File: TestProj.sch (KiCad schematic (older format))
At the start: 28 parts, among them SW1 SW_Push, U1 ATmega32U4-AU, Y1 16MHz

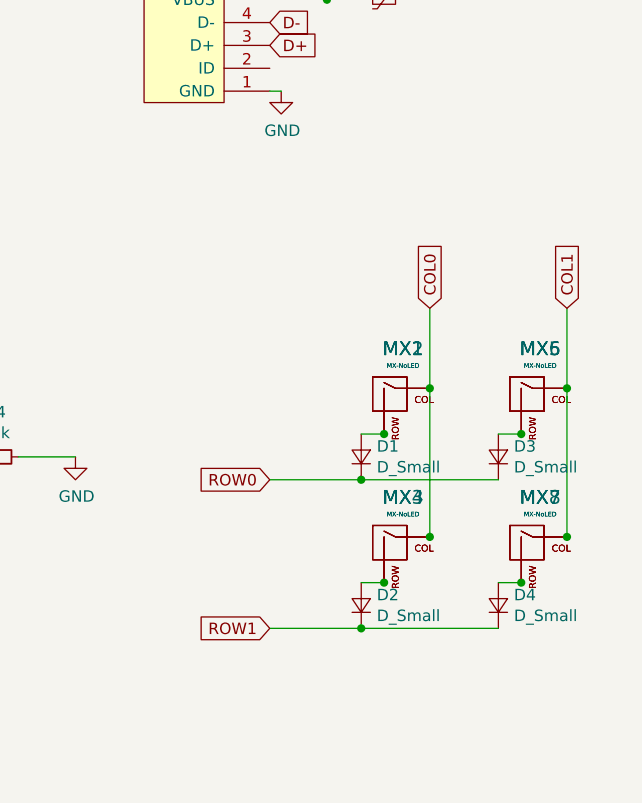
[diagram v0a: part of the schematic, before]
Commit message: fix dupe switches
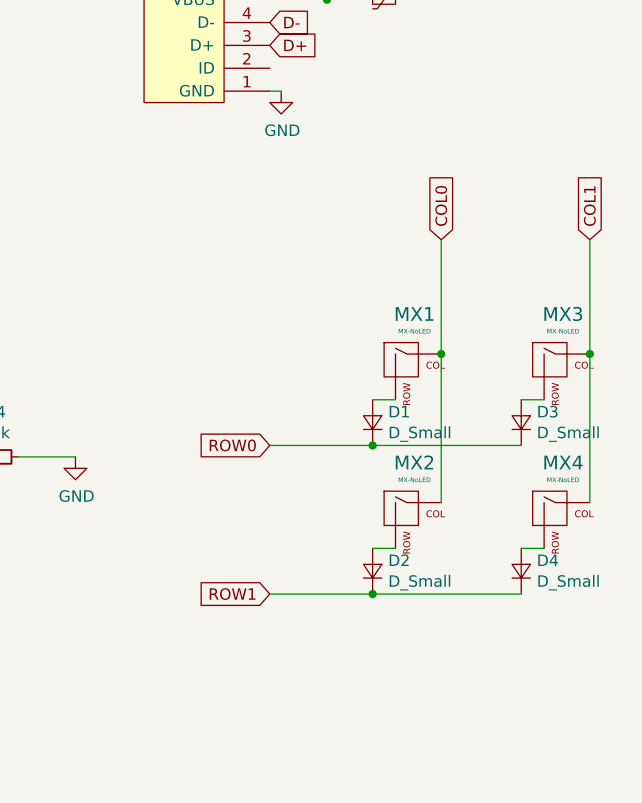
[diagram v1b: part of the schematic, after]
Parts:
- removed MX5, MX6, MX7, MX8: MX-NoLED, MX_Only:MXOnly-1U, symbol MX_Alps_Hybrid:MX-NoLED
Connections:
- net COL0: no longer MX3.1 (COL), MX4.1 (COL)
- net COL1: now also MX3.1 (COL), MX4.1 (COL)
- net at D1.2 (A), MX1.2 (ROW): no longer MX2.2 (ROW)
- net at D4.2 (A): now also MX4.2 (ROW)
- net at D3.2 (A): now also MX3.2 (ROW)
- new net: D2.2 (A), MX2.2 (ROW)
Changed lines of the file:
@@
 Wire Wire Line
 	7000 2750 7050 2750
-Connection ~ 7500 4900
+$Comp
+L MX_Alps_Hybrid:MX-NoLED MX1
+U 1 1 5D524996
+P 7600 3950
+F 0 "MX1" H 7633 4173 60  0000 C CNN
+F 1 "MX-NoLED" H 7633 4099 20  0000 C CNN
+F 2 "MX_Only:MXOnly-1U" H 6975 3925 60  0001 C CNN
+F 3 "" H 6975 3925 60  0001 C CNN
+	1    7600 3950
+	1    0    0    -1
+$EndComp
+$Comp
+L Device:D_Small D1
+U 1 1 5D52500E
+P 7450 4200
+F 0 "D1" V 7496 4132 50  0000 R CNN
+F 1 "D_Small" V 7405 4132 50  0000 R CNN
+F 2 "Diode_SMD:D_SOD-123" V 7450 4200 50  0001 C CNN
+F 3 "~" V 7450 4200 50  0001 C CNN
+	1    7450 4200
+	0    -1   -1   0
+$EndComp
+Wire Wire Line
+	7550 4100 7450 4100
+$Comp
+L MX_Alps_Hybrid:MX-NoLED MX2
+U 1 1 5D526ECD
+P 7600 4600
+F 0 "MX2" H 7633 4823 60  0000 C CNN
+F 1 "MX-NoLED" H 7633 4749 20  0000 C CNN
+F 2 "MX_Only:MXOnly-1U" H 6975 4575 60  0001 C CNN
+F 3 "" H 6975 4575 60  0001 C CNN
+	1    7600 4600
+	1    0    0    -1
+$EndComp
+$Comp
+L Device:D_Small D2
+U 1 1 5D526ED7
+P 7450 4850
+F 0 "D2" V 7496 4782 50  0000 R CNN
+F 1 "D_Small" V 7405 4782 50  0000 R CNN
+F 2 "Diode_SMD:D_SOD-123" V 7450 4850 50  0001 C CNN
+F 3 "~" V 7450 4850 50  0001 C CNN
+	1    7450 4850
+	0    -1   -1   0
+$EndComp
+Wire Wire Line
+	7550 4750 7450 4750
+$Comp
+L MX_Alps_Hybrid:MX-NoLED MX3
+U 1 1 5D528B54
+P 8250 3950
+F 0 "MX3" H 8283 4173 60  0000 C CNN
+F 1 "MX-NoLED" H 8283 4099 20  0000 C CNN
+F 2 "MX_Only:MXOnly-1U" H 7625 3925 60  0001 C CNN
+F 3 "" H 7625 3925 60  0001 C CNN
+	1    8250 3950
+	1    0    0    -1
+$EndComp
+$Comp
+L Device:D_Small D3
+U 1 1 5D528B5E
+P 8100 4200
+F 0 "D3" V 8146 4132 50  0000 R CNN
+F 1 "D_Small" V 8055 4132 50  0000 R CNN
+F 2 "Diode_SMD:D_SOD-123" V 8100 4200 50  0001 C CNN
+F 3 "~" V 8100 4200 50  0001 C CNN
+	1    8100 4200
+	0    -1   -1   0
+$EndComp
+Wire Wire Line
+	8200 4100 8100 4100
 $Comp
 L MX_Alps_Hybrid:MX-NoLED MX4
-U 1 1 5D4EFD87
-P 7550 4750
-F 0 "MX4" H 7583 4973 60  0000 C CNN
-F 1 "MX-NoLED" H 7583 4899 20  0000 C CNN
-F 2 "MX_Only:MXOnly-1U" H 6925 4725 60  0001 C CNN
-F 3 "" H 6925 4725 60  0001 C CNN
-	1    7550 4750
+U 1 1 5D528B69
+P 8250 4600
+F 0 "MX4" H 8283 4823 60  0000 C CNN
+F 1 "MX-NoLED" H 8283 4749 20  0000 C CNN
+F 2 "MX_Only:MXOnly-1U" H 7625 4575 60  0001 C CNN
+F 3 "" H 7625 4575 60  0001 C CNN
+	1    8250 4600
 	1    0    0    -1
 $EndComp
-Wire Wire Line
-	7500 4900 7400 4900
 $Comp
-L Device:D_Small D2
-U 1 1 5D4EFD7C
-P 7400 5000
-F 0 "D2" V 7446 4932 50  0000 R CNN
-F 1 "D_Small" V 7355 4932 50  0000 R CNN
-F 2 "Diode_SMD:D_SOD-123" V 7400 5000 50  0001 C CNN
-F 3 "~" V 7400 5000 50  0001 C CNN
-	1    7400 5000
+L Device:D_Small D4
+U 1 1 5D528B73
+P 8100 4850
+F 0 "D4" V 8146 4782 50  0000 R CNN
+F 1 "D_Small" V 8055 4782 50  0000 R CNN
+F 2 "Diode_SMD:D_SOD-123" V 8100 4850 50  0001 C CNN
+F 3 "~" V 8100 4850 50  0001 C CNN
+	1    8100 4850
 	0    -1   -1   0
 $EndComp
-$Comp
-L MX_Alps_Hybrid:MX-NoLED MX3
-U 1 1 5D4EFD72
-P 7550 4750
-F 0 "MX3" H 7583 4973 60  0000 C CNN
-F 1 "MX-NoLED" H 7583 4899 20  0000 C CNN
-F 2 "MX_Only:MXOnly-1U" H 6925 4725 60  0001 C CNN
-F 3 "" H 6925 4725 60  0001 C CNN
-	1    7550 4750
-	1    0    0    -1
-$EndComp
-Connection ~ 7500 4250
-$Comp
-L MX_Alps_Hybrid:MX-NoLED MX2
-U 1 1 5D4EC485
-P 7550 4100
-F 0 "MX2" H 7583 4323 60  0000 C CNN
-F 1 "MX-NoLED" H 7583 4249 20  0000 C CNN
-F 2 "MX_Only:MXOnly-1U" H 6925 4075 60  0001 C CNN
-F 3 "" H 6925 4075 60  0001 C CNN
-	1    7550 4100
-	1    0    0    -1
-$EndComp
 Wire Wire Line
-	7500 4250 7400 4250
-$Comp
-L Device:D_Small D1
-U 1 1 5D4E8C12
-P 7400 4350
-F 0 "D1" V 7446 4282 50  0000 R CNN
-F 1 "D_Small" V 7355 4282 50  0000 R CNN
-F 2 "Diode_SMD:D_SOD-123" V 7400 4350 50  0001 C CNN
-F 3 "~" V 7400 4350 50  0001 C CNN
-	1    7400 4350
-	0    -1   -1   0
-$EndComp
-$Comp
-L MX_Alps_Hybrid:MX-NoLED MX1
-U 1 1 5D4E72E5
-P 7550 4100
-F 0 "MX1" H 7583 4323 60  0000 C CNN
-F 1 "MX-NoLED" H 7583 4249 20  0000 C CNN
-F 2 "MX_Only:MXOnly-1U" H 6925 4075 60  0001 C CNN
-F 3 "" H 6925 4075 60  0001 C CNN
-	1    7550 4100
-	1    0    0    -1
-$EndComp
-Connection ~ 8100 4900
-$Comp
-L MX_Alps_Hybrid:MX-NoLED MX7
-U 1 1 5D4FC0A0
-P 8150 4750
-F 0 "MX7" H 8183 4973 60  0000 C CNN
-F 1 "MX-NoLED" H 8183 4899 20  0000 C CNN
-F 2 "MX_Only:MXOnly-1U" H 7525 4725 60  0001 C CNN
-F 3 "" H 7525 4725 60  0001 C CNN
-	1    8150 4750
-	1    0    0    -1
-$EndComp
+	8200 4750 8100 4750
 Wire Wire Line
-	8100 4900 8000 4900
-$Comp
-L Device:D_Small D4
-U 1 1 5D4FC0AB
-P 8000 5000
-F 0 "D4" V 8046 4932 50  0000 R CNN
-F 1 "D_Small" V 7955 4932 50  0000 R CNN
-F 2 "Diode_SMD:D_SOD-123" V 8000 5000 50  0001 C CNN
-F 3 "~" V 8000 5000 50  0001 C CNN
-	1    8000 5000
-	0    -1   -1   0
-$EndComp
-$Comp
-L MX_Alps_Hybrid:MX-NoLED MX8
-U 1 1 5D4FC0B5
-P 8150 4750
-F 0 "MX8" H 8183 4973 60  0000 C CNN
-F 1 "MX-NoLED" H 8183 4899 20  0000 C CNN
-F 2 "MX_Only:MXOnly-1U" H 7525 4725 60  0001 C CNN
-F 3 "" H 7525 4725 60  0001 C CNN
-	1    8150 4750
-	1    0    0    -1
-$EndComp
-Connection ~ 8100 4250
-$Comp
-L MX_Alps_Hybrid:MX-NoLED MX5
-U 1 1 5D4FC0C0
-P 8150 4100
-F 0 "MX5" H 8183 4323 60  0000 C CNN
-F 1 "MX-NoLED" H 8183 4249 20  0000 C CNN
-F 2 "MX_Only:MXOnly-1U" H 7525 4075 60  0001 C CNN
-F 3 "" H 7525 4075 60  0001 C CNN
-	1    8150 4100
-	1    0    0    -1
-$EndComp
+	7750 3400 7750 3900
+Connection ~ 7750 3900
 Wire Wire Line
-	8100 4250 8000 4250
-$Comp
-L Device:D_Small D3
-U 1 1 5D4FC0CB
-P 8000 4350
-F 0 "D3" V 8046 4282 50  0000 R CNN
-F 1 "D_Small" V 7955 4282 50  0000 R CNN
-F 2 "Diode_SMD:D_SOD-123" V 8000 4350 50  0001 C CNN
-F 3 "~" V 8000 4350 50  0001 C CNN
-	1    8000 4350
-	0    -1   -1   0
-$EndComp
-$Comp
-L MX_Alps_Hybrid:MX-NoLED MX6
-U 1 1 5D4FC0D5
-P 8150 4100
-F 0 "MX6" H 8183 4323 60  0000 C CNN
-F 1 "MX-NoLED" H 8183 4249 20  0000 C CNN
-F 2 "MX_Only:MXOnly-1U" H 7525 4075 60  0001 C CNN
-F 3 "" H 7525 4075 60  0001 C CNN
-	1    8150 4100
-	1    0    0    -1
-$EndComp
+	7750 3900 7750 4550
 Wire Wire Line
-	7700 3700 7700 4050
-Connection ~ 7700 4700
-Connection ~ 7700 4050
+	8400 3400 8400 3900
+Connection ~ 8400 3900
 Wire Wire Line
-	7700 4050 7700 4700
+	8400 3900 8400 4550
 Wire Wire Line
-	8000 4450 7400 4450
-Connection ~ 7400 4450
+	8100 4300 7450 4300
+Connection ~ 7450 4300
 Wire Wire Line
-	7400 4450 7000 4450
+	7450 4300 7000 4300
 Wire Wire Line
-	8000 5100 7400 5100
-Connection ~ 7400 5100
+	8100 4950 7450 4950
+Connection ~ 7450 4950
 Wire Wire Line
-	7400 5100 7000 5100
-Wire Wire Line
-	8300 3700 8300 4050
-Connection ~ 8300 4700
-Connection ~ 8300 4050
-Wire Wire Line
-	8300 4050 8300 4700
-Text GLabel 7700 3700 1    50   Input ~ 0
+	7450 4950 7000 4950
+Text GLabel 7750 3400 1    50   Input ~ 0
 COL0
-Text GLabel 8300 3700 1    50   Input ~ 0
+Text GLabel 8400 3400 1    50   Input ~ 0
 COL1
-Text GLabel 7000 4450 0    50   Input ~ 0
+Text GLabel 7000 4300 0    50   Input ~ 0
 ROW0
-Text GLabel 7000 5100 0    50   Input ~ 0
+Text GLabel 7000 4950 0    50   Input ~ 0
 ROW1
 $EndSCHEMATC

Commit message: starting from scratch with atmega32u2
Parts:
- removed C4: 22pF, Capacitor_SMD:C_0805_2012Metric, symbol Device:C_Small
- removed C5: 0.1uF, Capacitor_SMD:C_0805_2012Metric, symbol Device:C_Small
- removed C6: 10uF, Capacitor_SMD:C_0805_2012Metric, symbol Device:C_Small
- removed C7: 1uF, Capacitor_SMD:C_0805_2012Metric, symbol Device:C_Small
- removed R4: 10k, Resistor_SMD:R_0805_2012Metric, symbol Device:R_Small
- removed U1: ATmega32U4-AU, Package_QFP:TQFP-44_10x10mm_P0.8mm, symbol MCU_Microchip_ATmega:ATmega32U4-AU
- added U1: ATmega32U2-AU, Package_QFP:TQFP-32_7x7mm_P0.8mm, symbol MCU_Microchip_ATmega:ATmega32U2-AU
- C1, C2: value 0.1uF -> 22pF; footprint Capacitor_SMD:C_0805_2012Metric -> Capacitor_SMD:C_0805_2012Metric_Pad1.15x1.40mm_HandSolder
- C3: value 22pF -> 1uF; footprint Capacitor_SMD:C_0805_2012Metric -> Capacitor_SMD:C_0805_2012Metric_Pad1.15x1.40mm_HandSolder
- MX1, MX2, MX3, MX4: symbol MX_Alps_Hybrid:MX-NoLED -> TestProj-rescue:MX-NoLED-MX_Alps_Hybrid
- R1, R2, R3: footprint Resistor_SMD:R_0805_2012Metric -> Resistor_SMD:R_0805_2012Metric_Pad1.15x1.40mm_HandSolder
- USB1: symbol random-keyboard-parts:Molex-0548190589 -> TestProj-rescue:Molex-0548190589-random-keyboard-parts
- Y1: footprint Crystal:Crystal_SMD_3225-4Pin_3.2x2.5mm -> Crystal:Crystal_SMD_3225-4Pin_3.2x2.5mm_HandSoldering
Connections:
- net +5V: now also U1.31 (UVCC), U1.32 (AVCC), U1.4 (VCC); no longer C1.1, C2.1
- net D-: now also R1.1; no longer R1.2
- net GND: now also C2.1, U1.28 (UGND), U1.3 (GND); no longer C2.2
- net at R3.2, SW1.2: now also U1.24 (PC1/~RESET)
- net at Y1.1: now also C1.1, U1.1 (XTAL1)
- net at Y1.3: now also C2.2, U1.2 (PC0/XTAL2); no longer C3.1
- net at R2.1: now also U1.29 (D+)
- new net: C3.1, U1.27 (UCAP)
- new net: R1.2, U1.30 (D-)
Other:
- moved on the sheet: D1, D2, D3, D4, F1, MX1, MX2, MX3, MX4, USB1

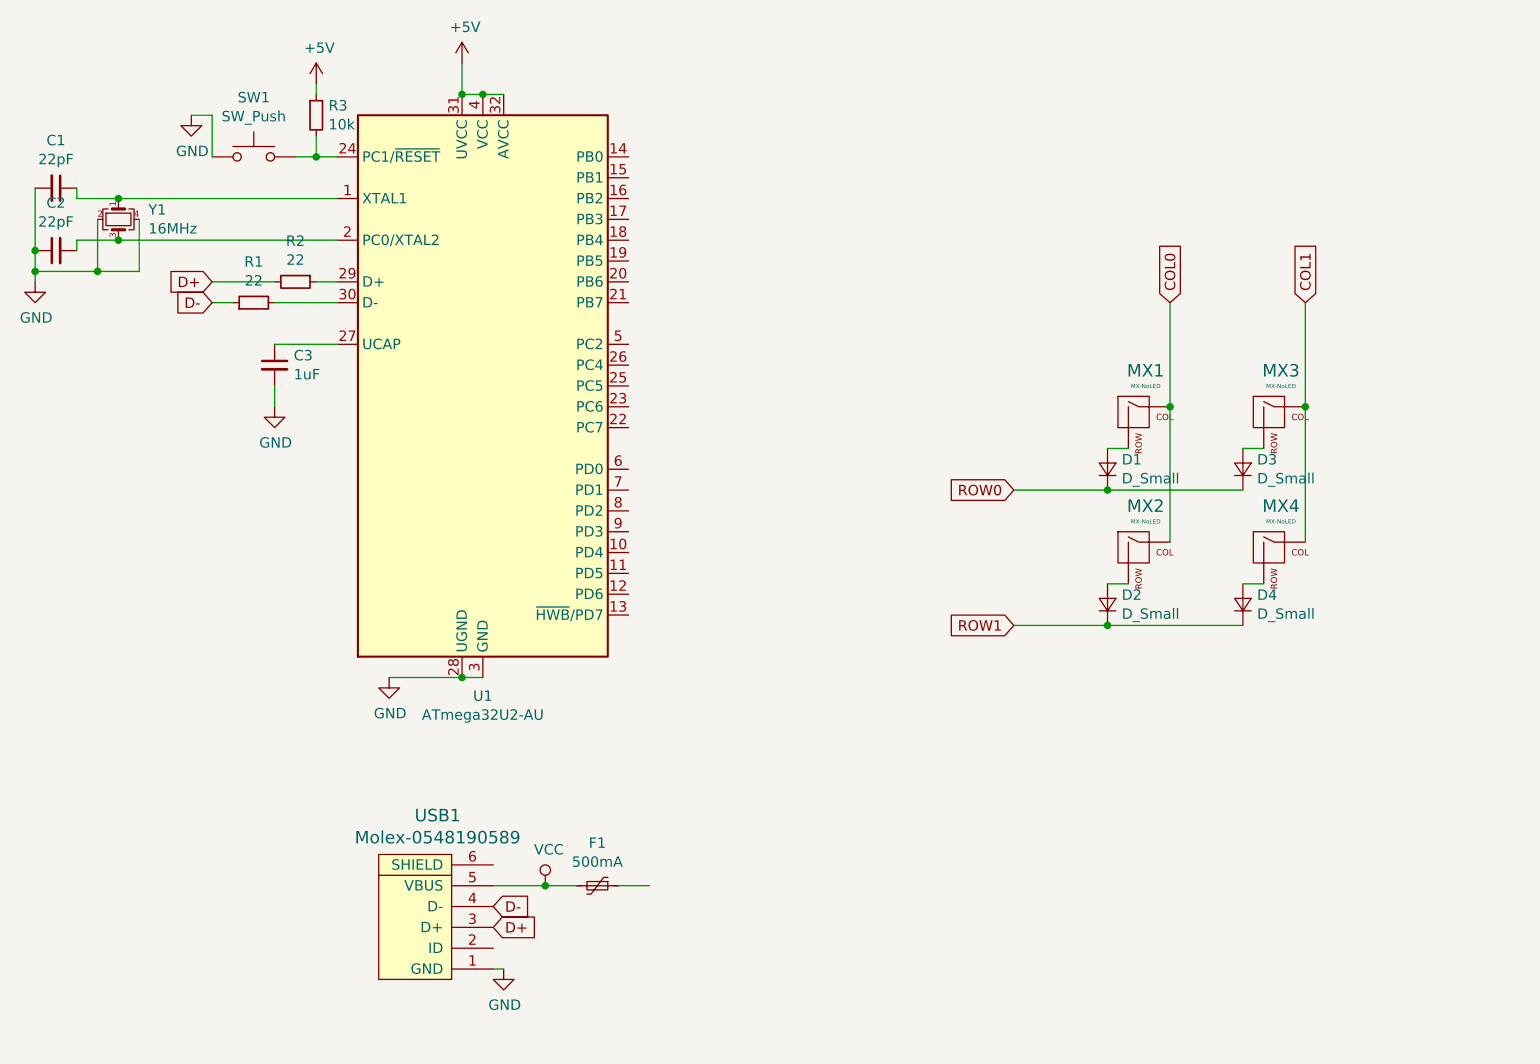
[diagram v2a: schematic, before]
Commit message: a poor routing job 8)
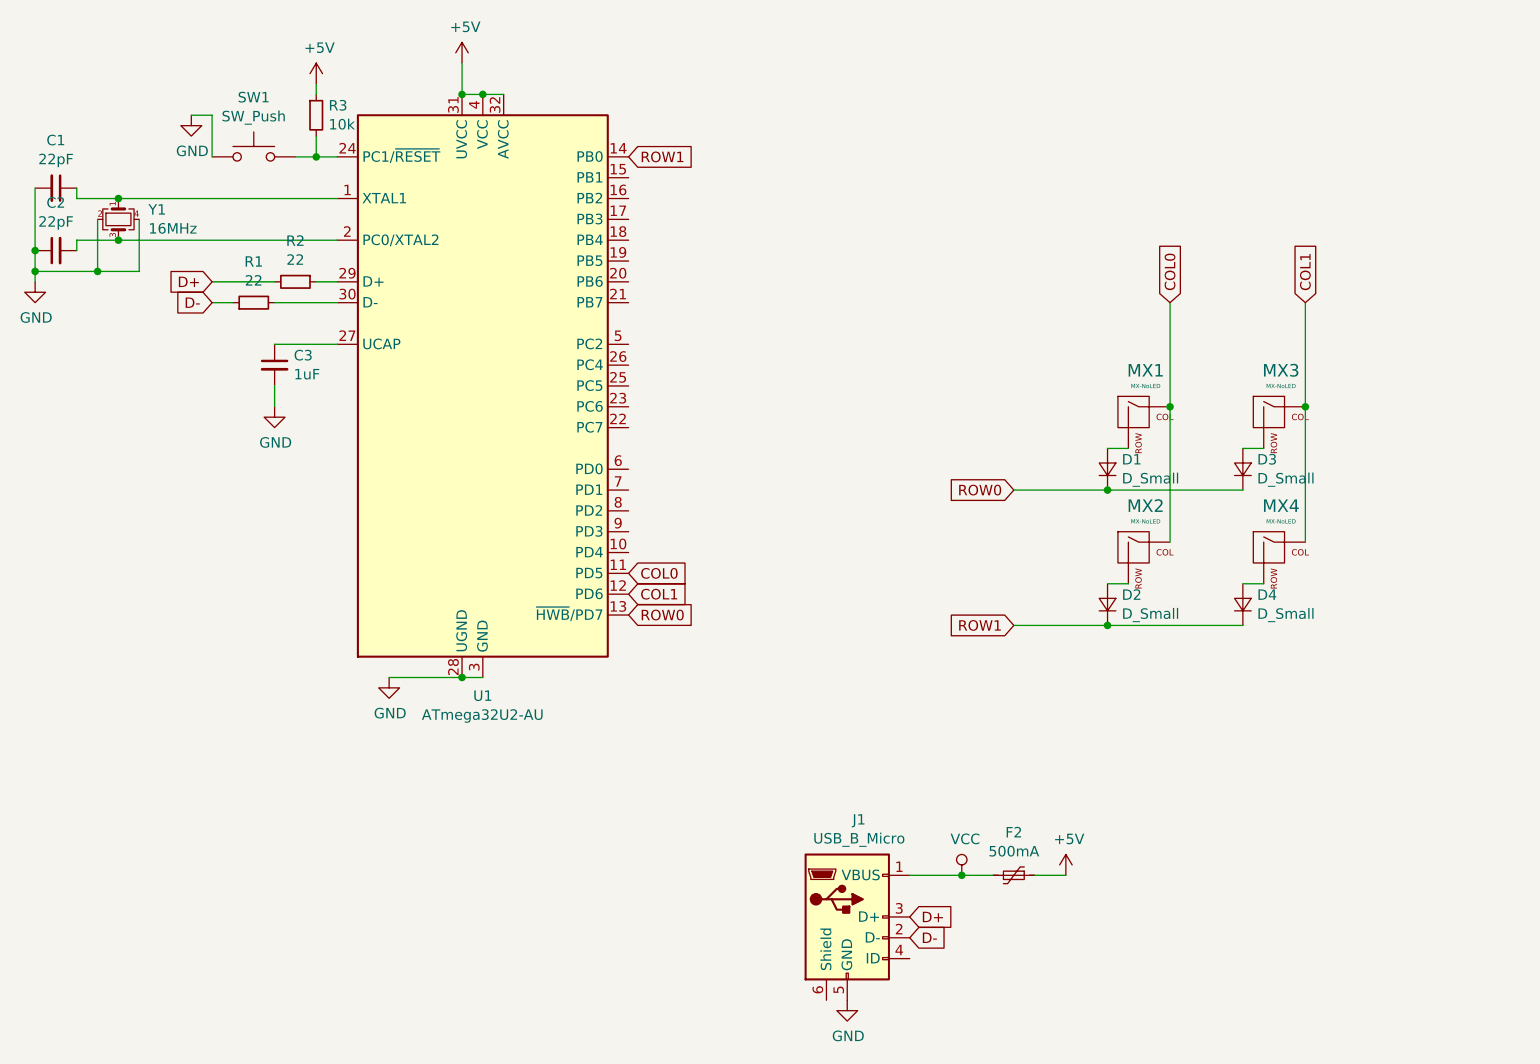
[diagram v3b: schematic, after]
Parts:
- removed F1: 500mA, Fuse:Fuse_1206_3216Metric, symbol Device:Polyfuse_Small
- removed USB1: Molex-0548190589, random-keyboard-parts:Molex-0548190589, symbol TestProj-rescue:Molex-0548190589-random-keyboard-parts
- added F2: 500mA, Fuse:Fuse_1206_3216Metric, symbol Device:Polyfuse_Small
- added J1: USB_B_Micro, Connector_USB:USB_Micro-B_Amphenol_10103594-0001LF_Horizontal, symbol Connector:USB_B_Micro
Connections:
- net +5V: now also F2.1
- net COL0: now also U1.11 (PD5)
- net COL1: now also U1.12 (PD6)
- net D+: now also J1.3 (D+)
- net D-: now also J1.2 (D-)
- net GND: now also J1.5 (GND)
- net ROW0: now also U1.13 (~HWB~/PD7)
- net ROW1: now also U1.14 (PB0)
- net VCC: now also F2.2, J1.1 (VBUS)
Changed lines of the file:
@@
 $EndDescr
-$Comp
-L Device:Polyfuse_Small F1
-U 1 1 5D4D98D0
-P 4100 5250
-F 0 "F1" V 3895 5250 50  0000 C CNN
-F 1 "500mA" V 3986 5250 50  0000 C CNN
-F 2 "Fuse:Fuse_1206_3216Metric" H 4150 5050 50  0001 L CNN
-F 3 "~" H 4100 5250 50  0001 C CNN
-	1    4100 5250
-	0    1    1    0
-$EndComp
-$Comp
-L power:VCC #PWR0111
-U 1 1 5D4DA718
-P 3850 5250
-F 0 "#PWR0111" H 3850 5100 50  0001 C CNN
-F 1 "VCC" H 3867 5423 50  0000 C CNN
-F 2 "" H 3850 5250 50  0001 C CNN
-F 3 "" H 3850 5250 50  0001 C CNN
-	1    3850 5250
-	1    0    0    -1
-$EndComp
-Wire Wire Line
-	4200 5250 4350 5250
-Wire Wire Line
-	3850 5250 4000 5250
 $Comp
 L TestProj-rescue:MX-NoLED-MX_Alps_Hybrid MX1
@@
 Connection ~ 6550 4000
 Connection ~ 6550 3350
-Connection ~ 3850 5250
 Text GLabel 6100 4000 0    50   Input ~ 0
 ROW1
@@
 Wire Wire Line
 	6550 3350 6100 3350
-Wire Wire Line
-	3600 5650 3650 5650
-$Comp
-L power:GND #PWR0112
-U 1 1 5D4E24B4
-P 3650 5650
-F 0 "#PWR0112" H 3650 5400 50  0001 C CNN
-F 1 "GND" H 3655 5477 50  0000 C CNN
-F 2 "" H 3650 5650 50  0001 C CNN
-F 3 "" H 3650 5650 50  0001 C CNN
-	1    3650 5650
-	1    0    0    -1
-$EndComp
-Text GLabel 3600 5450 2    50   Input ~ 0
-D+
-Text GLabel 3600 5350 2    50   Input ~ 0
-D-
-Wire Wire Line
-	3600 5250 3850 5250
-$Comp
-L TestProj-rescue:Molex-0548190589-random-keyboard-parts USB1
-U 1 1 5D4D5338
-P 3300 5450
-F 0 "USB1" V 3837 5417 60  0000 C CNN
-F 1 "Molex-0548190589" V 3731 5417 60  0000 C CNN
-F 2 "random-keyboard-parts:Molex-0548190589" H 3300 5450 60  0001 C CNN
-F 3 "" H 3300 5450 60  0001 C CNN
-	1    3300 5450
-	0    -1   -1   0
-$EndComp
 $Comp
 L MCU_Microchip_ATmega:ATmega32U2-AU U1
@@
 Text GLabel 2250 2350 0    50   Input ~ 0
 D+
+Text GLabel 4250 3750 2    50   Input ~ 0
+COL0
+$Comp
+L Connector:USB_B_Micro J1
+U 1 1 5D50024F
+P 5300 5400
+F 0 "J1" H 5357 5867 50  0000 C CNN
+F 1 "USB_B_Micro" H 5357 5776 50  0000 C CNN
+F 2 "Connector_USB:USB_Micro-B_Amphenol_10103594-0001LF_Horizontal" H 5450 5350 50  0001 C CNN
+F 3 "~" H 5450 5350 50  0001 C CNN
+	1    5300 5400
+	1    0    0    -1
+$EndComp
+$Comp
+L Device:Polyfuse_Small F2
+U 1 1 5D506659
+P 6100 5200
+F 0 "F2" V 5895 5200 50  0000 C CNN
+F 1 "500mA" V 5986 5200 50  0000 C CNN
+F 2 "Fuse:Fuse_1206_3216Metric" H 6150 5000 50  0001 L CNN
+F 3 "~" H 6100 5200 50  0001 C CNN
+	1    6100 5200
+	0    1    1    0
+$EndComp
+$Comp
+L power:VCC #PWR0107
+U 1 1 5D50665F
+P 5850 5200
+F 0 "#PWR0107" H 5850 5050 50  0001 C CNN
+F 1 "VCC" H 5867 5373 50  0000 C CNN
+F 2 "" H 5850 5200 50  0001 C CNN
+F 3 "" H 5850 5200 50  0001 C CNN
+	1    5850 5200
+	1    0    0    -1
+$EndComp
+Wire Wire Line
+	6200 5200 6350 5200
+Wire Wire Line
+	5850 5200 6000 5200
+Connection ~ 5850 5200
+Wire Wire Line
+	5600 5200 5850 5200
+Text GLabel 5600 5500 2    50   Input ~ 0
+D-
+Text GLabel 5600 5400 2    50   Input ~ 0
+D+
+$Comp
+L power:GND #PWR0108
+U 1 1 5D50758A
+P 5300 5800
+F 0 "#PWR0108" H 5300 5550 50  0001 C CNN
+F 1 "GND" H 5305 5627 50  0000 C CNN
+F 2 "" H 5300 5800 50  0001 C CNN
+F 3 "" H 5300 5800 50  0001 C CNN
+	1    5300 5800
+	1    0    0    -1
+$EndComp
+$Comp
+L power:+5V #PWR0109
+U 1 1 5D51C4E0
+P 6350 5200
+F 0 "#PWR0109" H 6350 5050 50  0001 C CNN
+F 1 "+5V" H 6365 5373 50  0000 C CNN
+F 2 "" H 6350 5200 50  0001 C CNN
+F 3 "" H 6350 5200 50  0001 C CNN
+	1    6350 5200
+	1    0    0    -1
+$EndComp
+Text GLabel 4250 3850 2    50   Input ~ 0
+COL1
+Text GLabel 4250 3950 2    50   Input ~ 0
+ROW0
+Text GLabel 4250 1750 2    50   Input ~ 0
+ROW1
 $EndSCHEMATC
